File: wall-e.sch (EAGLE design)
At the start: 10 parts, among them IC1 VREG-TS1117CW-3V3, Q1 BC850SMD, Q2 BC850SMD, Q3 BC850SMD, Q4 BC850SMD, Q5 BC850SMD

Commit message: Second part of the schematic
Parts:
- removed Q1, Q2, Q3, Q4, Q5: BC850SMD, transistor-npn:BC850SMD
- added C3, C4, C5, C6, C7, C8: (no value), rcl:C-EUC0805
- added CODEUSE: (no value), con-amp:SMDTOP-4
- added D1, D2, D3, D4, D5, D6, D7: (no value), diode:DIODE-SOD323-R
- added JP1: (no value), pinhead:PINHD-2X5
- added LED5: (no value), led:LEDCHIP-LED0805
- added PNEUMATIC: (no value), con-amp:SMDTOP-8
- added R1, R2, R3, R4, R5: (no value), rcl:R-US_R0805
- added TOIT: (no value), con-amp:SMDTOP-12
- added U1, U2, U3, U4, U5: TSM2306CX, tsm2306:TSM2306CX
- added X1: (no value), con-amp:SMDTOP-6
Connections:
- net N$1 renamed IMU_SCL
- net N$2 renamed IMU_SDA
- removed net N$3: Q3.B, U$1.PA5
- removed net N$4: Q2.B, U$1.PB0
- new net AX12-RX: JP1.8, U$1.PA10
- new net AX12-TX: JP1.10, U$1.PA9
- new net BUTTON1: TOIT-2.1, U$1.PA15
- new net BUTTON2: TOIT-3.1, U$1.PB3
- new net BUTTON3: TOIT-4.1, U$1.PB4
- new net BUTTON4: TOIT-5.1, U$1.PB5
- new net CODEUSE1_TIM1: CODEUSE-1.1, U$1.PA6
- new net CODEUSE1_TIM2: CODEUSE-2.1, U$1.PA7
- new net CODEUSE2_TIM1: CODEUSE-3.1, U$1.PB14
- new net CODEUSE2_TIM2: CODEUSE-4.1, U$1.PB15
- new net JACK: TOIT-1.1, U$1.PA0
- new net LED1: TOIT-6.1, U$1.PF0/OSC_IN
- new net LED2: TOIT-7.1, U$1.PF1/OSC_OUT
- new net LED3: TOIT-8.1, U$1.PB8
- new net LED4: TOIT-9.1, U$1.PB9
- new net MCU_RESET: C3.1, U$1.NRST
- new net N$11: R1.2, U$1.BOOT0
- new net N$13: TOIT-10.1
- new net N$15: TOIT-11.1
- new net N$17: U$1.PA1
- new net N$8: D6.A, PNEUMATIC-2.1, U4.D
- new net N$9: D7.A, PNEUMATIC-7.1, U5.D
- new net PUMP: U$1.PA8, U5.G
- new net SENSOR1: U$1.PB12, X1-2.1
- new net SENSOR2: U$1.PB13, X1-3.1
- new net SENSOR3: U$1.PA11, X1-4.1
- new net SENSOR4: U$1.PA12, X1-5.1
- new net VALVE1: U$1.PA5, U4.G
- new net VALVE2: U$1.PB0, U1.G
- new net VALVE3: U$1.PB1, U2.G
- new net VALVE4: U$1.PB2, U3.G
- net +12V: now also D7.C, PNEUMATIC-8.1; no longer Q1.C
- net +5V: now also D1.C, D2.C, D3.C, D6.C, JP1.2, JP1.4, PNEUMATIC-1.1, X1-1.1; no longer Q2.C, Q3.C, Q4.C, Q5.C
- net GND: now also C3.2, JP1.6, JP1.9, R1.1, TOIT-12.1, U1.S, U2.S, U3.S, U4.S, U5.S, X1-6.1
- net N$5: now also D1.A, PNEUMATIC-3.1, U1.D; no longer Q4.B, U$1.PB1
- net N$6: now also D2.A, PNEUMATIC-4.1, U2.D; no longer Q5.B, U$1.PB2
- net N$7: now also D3.A, PNEUMATIC-5.1, U3.D; no longer Q1.B, U$1.PA8
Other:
- moved on the sheet: SV1

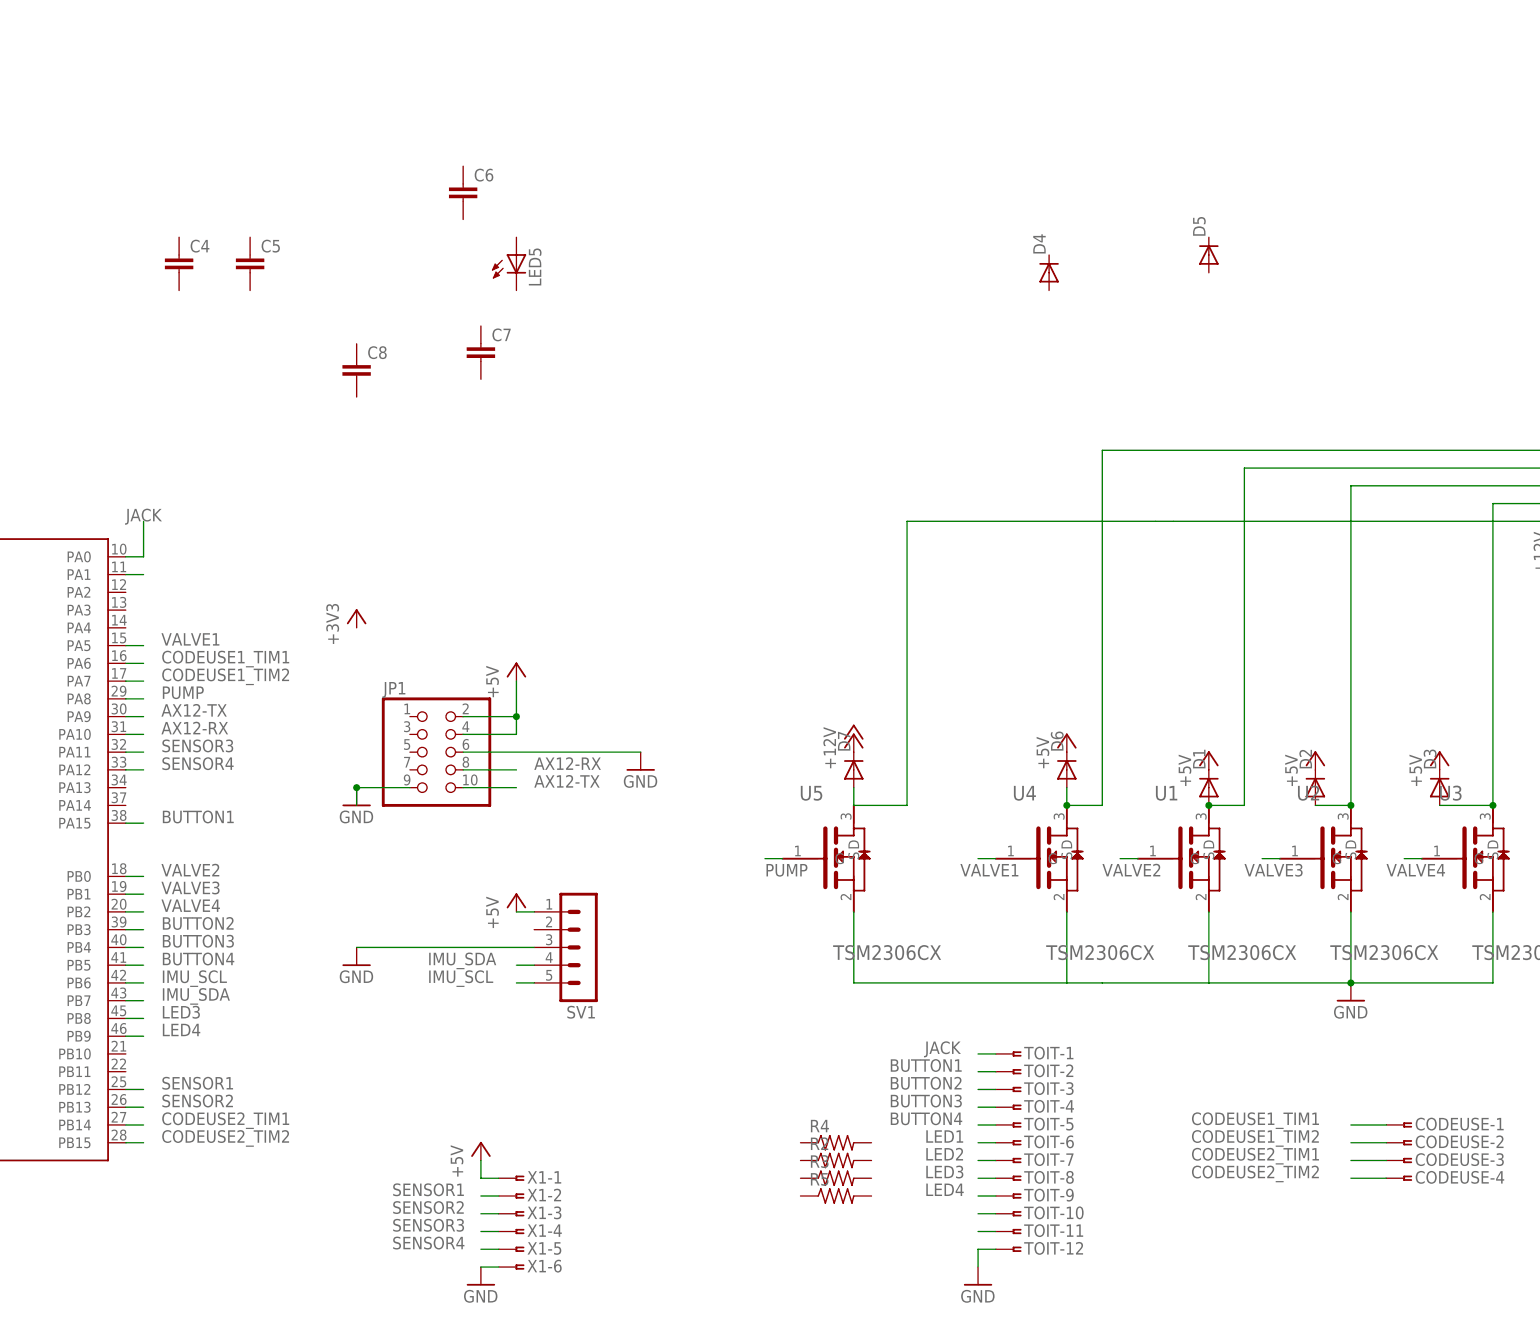
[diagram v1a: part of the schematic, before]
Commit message: Addition of connectors to control the motors.
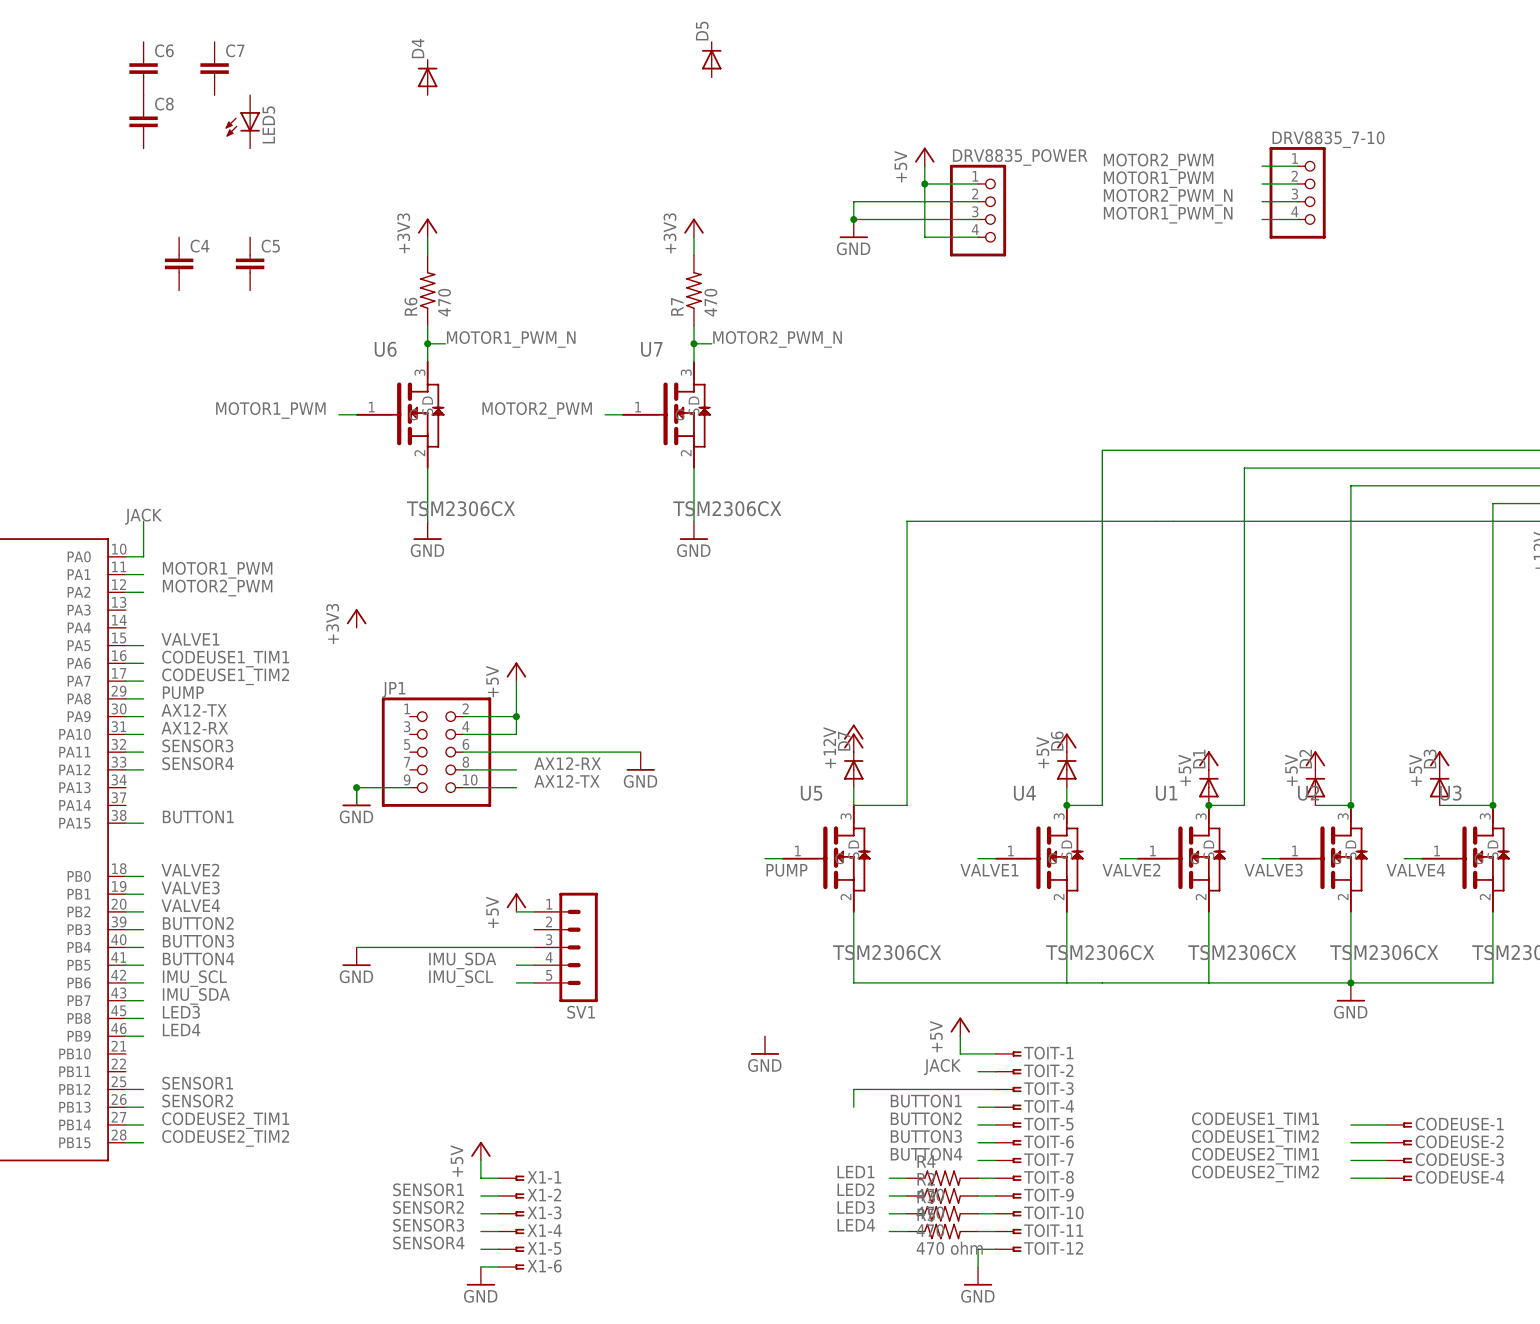
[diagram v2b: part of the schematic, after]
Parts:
- added DRV8835_7-10, DRV8835_POWER: (no value), pinhead:PINHD-1X4
- added R6, R7: 470, rcl:R-US_R0805
- added U6, U7: TSM2306CX, tsm2306:TSM2306CX
- R2, R3, R4: value (none) -> 470
- R5: value (none) -> 470 ohm
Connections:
- removed net N$13: TOIT-10.1
- removed net N$15: TOIT-11.1
- removed net N$17: U$1.PA1
- new net MOTOR1_PWM: DRV8835_7-10.2, U$1.PA1, U6.G
- new net MOTOR1_PWM_N: DRV8835_7-10.4, R6.1, U6.D
- new net MOTOR2_PWM: DRV8835_7-10.1, U$1.PA2, U7.G
- new net MOTOR2_PWM_N: DRV8835_7-10.3, R7.1, U7.D
- new net N$1: R5.2, TOIT-11.1
- new net N$10: C6.2, C8.1
- new net N$18: TOIT-3.1
- new net N$2: R3.2, TOIT-10.1
- new net N$3: R2.2, TOIT-9.1
- new net N$4: R4.2, TOIT-8.1
- net +3V3: now also R6.2, R7.2
- net +5V: now also DRV8835_POWER.1, DRV8835_POWER.4, TOIT-1.1
- net BUTTON1: now also TOIT-4.1; no longer TOIT-2.1
- net BUTTON2: now also TOIT-5.1; no longer TOIT-3.1
- net BUTTON3: now also TOIT-6.1; no longer TOIT-4.1
- net BUTTON4: now also TOIT-7.1; no longer TOIT-5.1
- net GND: now also DRV8835_POWER.2, DRV8835_POWER.3, U6.S, U7.S
- net JACK: now also TOIT-2.1; no longer TOIT-1.1
- net LED1: now also R4.1; no longer TOIT-6.1
- net LED2: now also R2.1; no longer TOIT-7.1
- net LED3: now also R3.1; no longer TOIT-8.1
- net LED4: now also R5.1; no longer TOIT-9.1
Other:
- moved on the sheet: C6, C7, C8, D4, D5, LED5, R2, R3, R4, R5

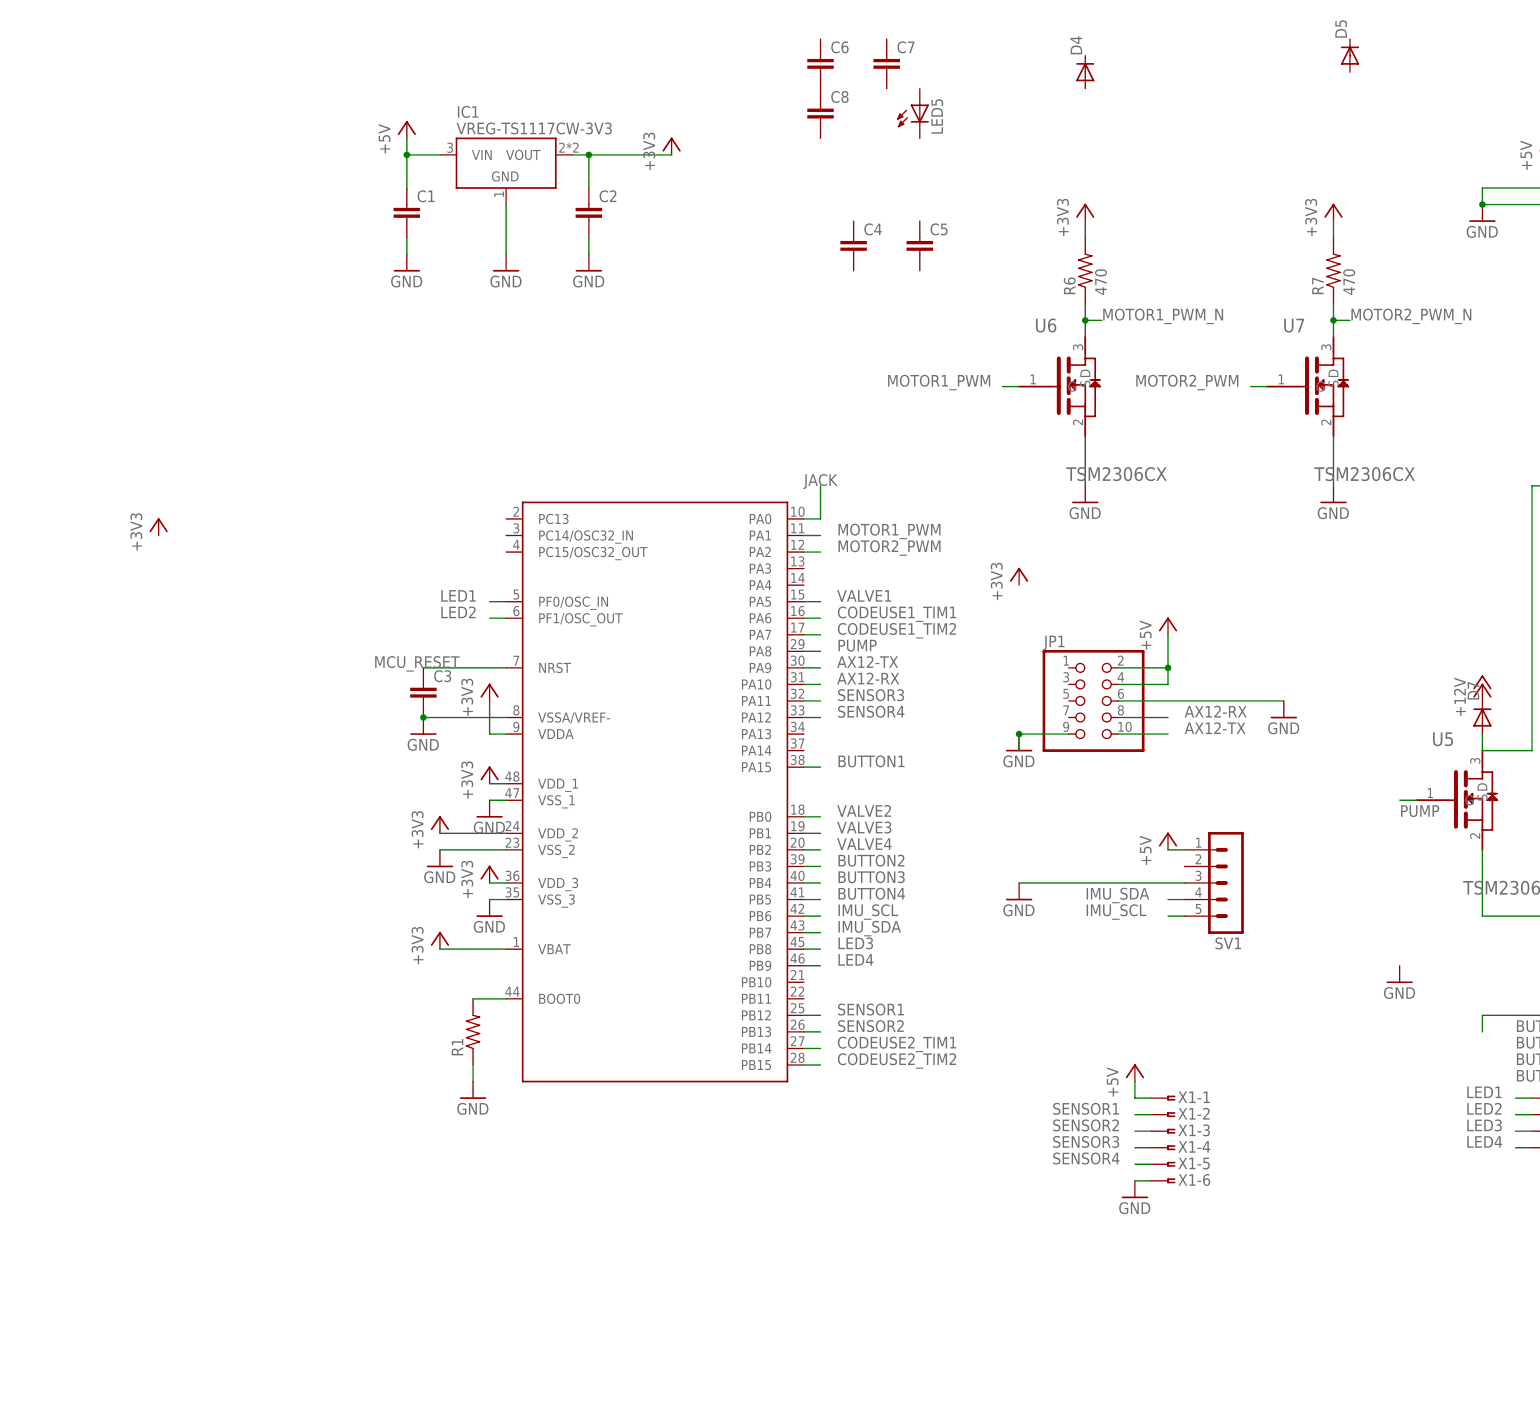
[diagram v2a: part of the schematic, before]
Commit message: SWD and decoupling capa
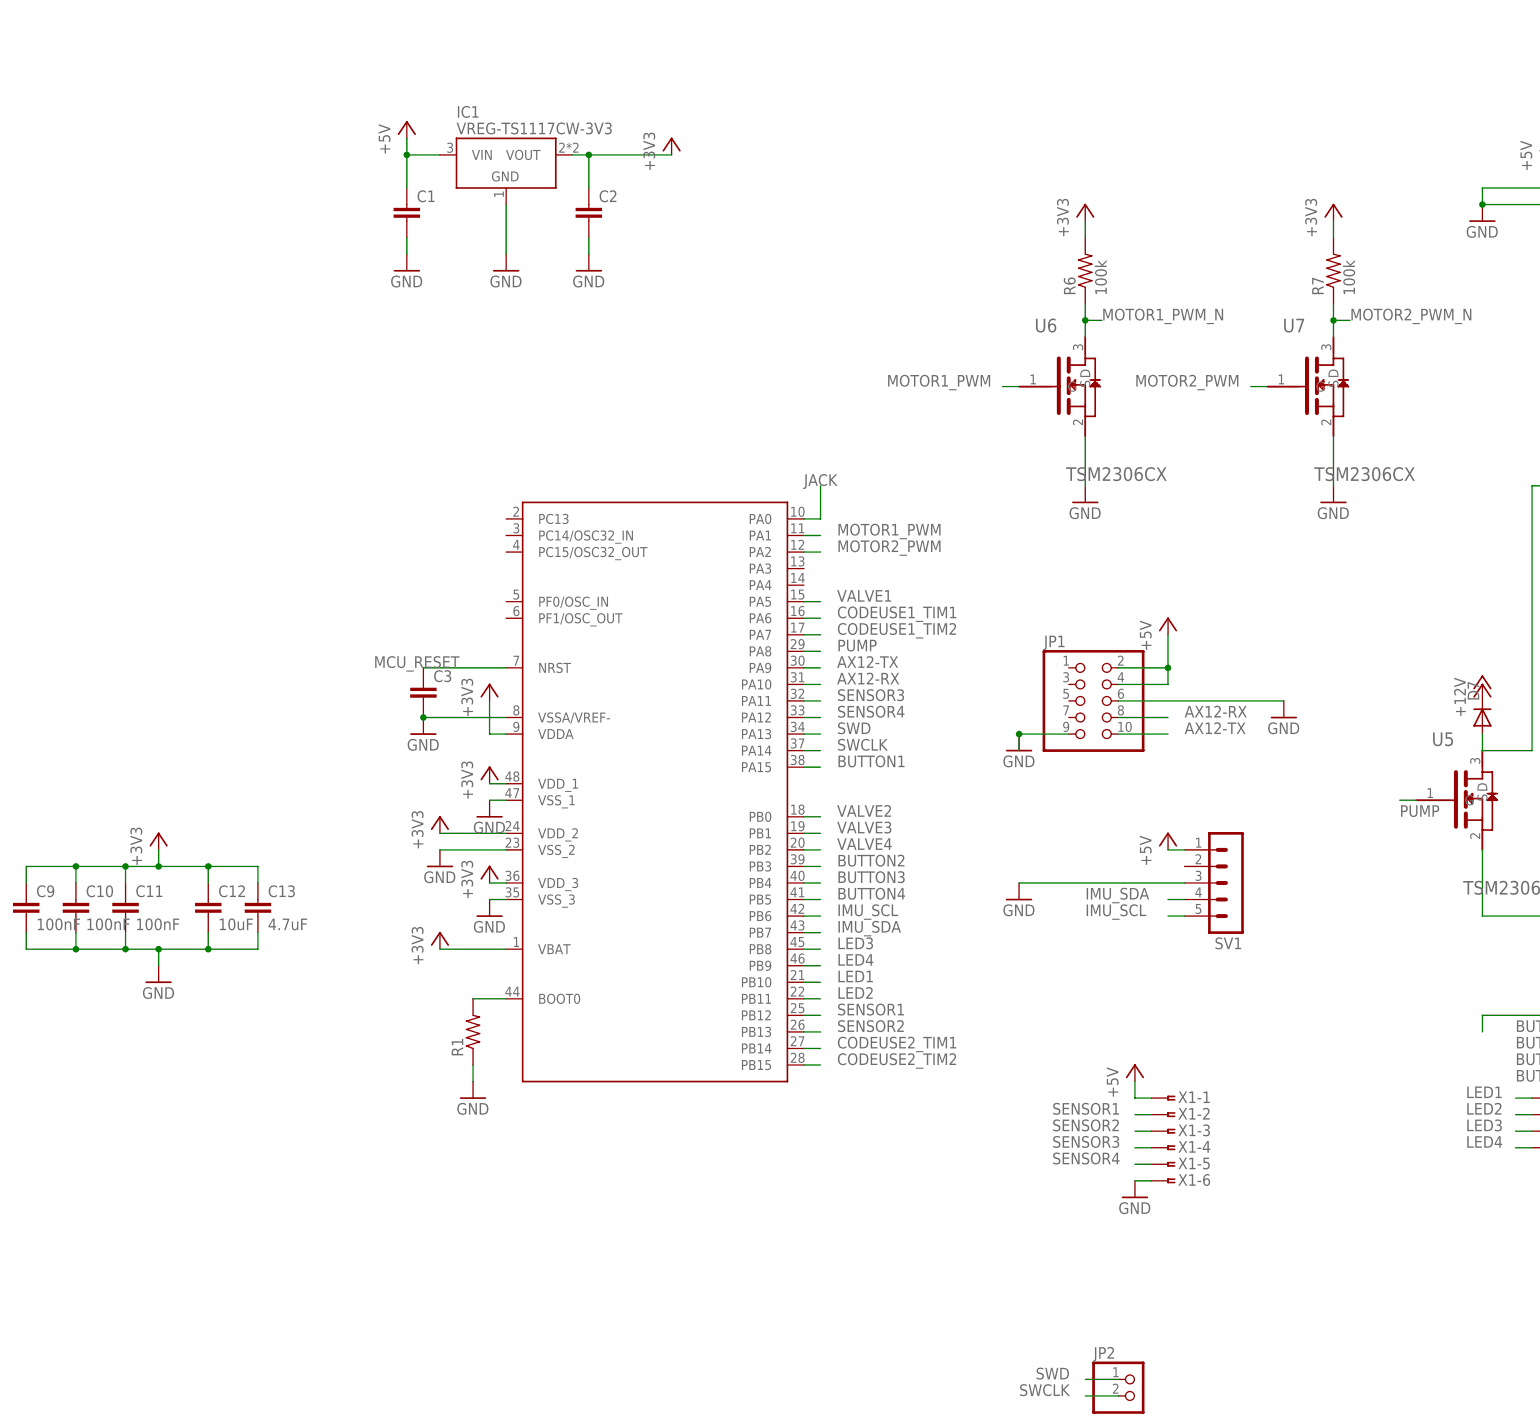
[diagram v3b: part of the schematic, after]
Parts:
- removed C4, C5, C6, C7, C8: (no value), rcl:C-EUC0805
- removed D4, D5: (no value), diode:DIODE-SOD323-R
- removed LED5: (no value), led:LEDCHIP-LED0805
- added C10, C11, C9: 100nF, rcl:C-EUC0805
- added C12: 10uF, rcl:C-EUC0805
- added C13: 4.7uF, rcl:C-EUC0805
- added JP2: (no value), pinhead:PINHD-1X2
- R6, R7: value 470 -> 100k
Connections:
- removed net N$10: C6.2, C8.1
- new net SWCLK: JP2.2, U$1.PA14
- new net SWD: JP2.1, U$1.PA13
- net +3V3: now also C10.1, C11.1, C12.1, C13.1, C9.1
- net GND: now also C10.2, C11.2, C12.2, C13.2, C9.2
- net LED1: now also U$1.PB10; no longer U$1.PF0/OSC_IN
- net LED2: now also U$1.PB11; no longer U$1.PF1/OSC_OUT
